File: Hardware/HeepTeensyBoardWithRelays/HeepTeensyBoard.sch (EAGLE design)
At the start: 40 parts, among them J1 MAGJACK, J4 POWER_JACKPTH, K1 RELAY-SPDT-JZC-11F, K2 RELAY-SPDT-JZC-11F, K3 RELAY-SPDT-JZC-11F, Q1 25MHz, U1 ENC28J60-SO

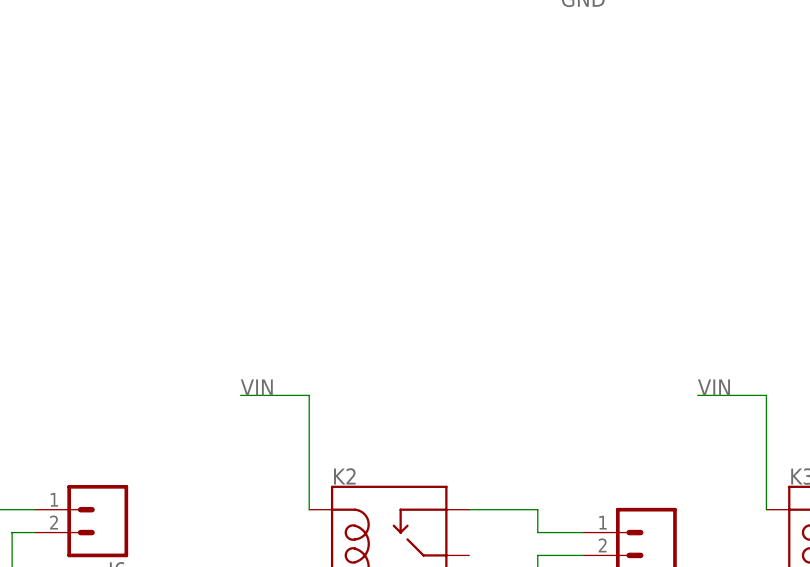
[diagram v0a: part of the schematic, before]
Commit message: #152 Added a label to the part of the schematic with AC inputs
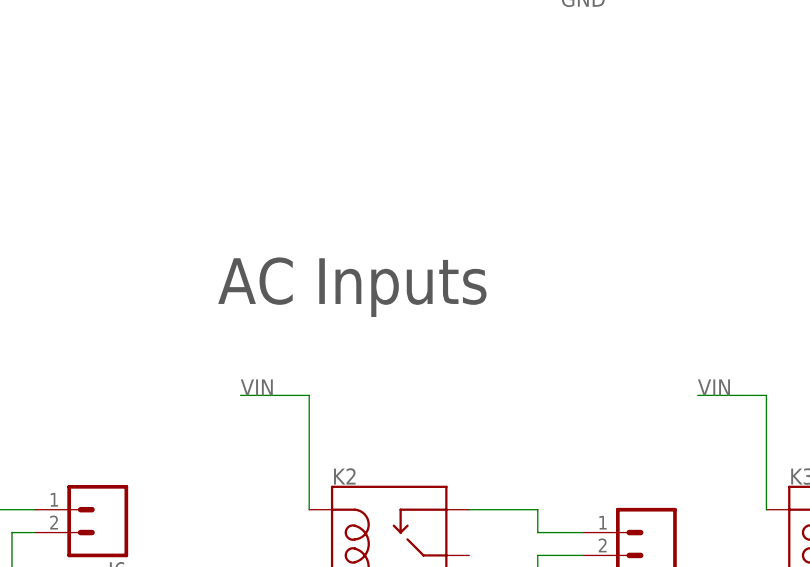
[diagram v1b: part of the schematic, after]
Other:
- note added: "AC Inputs"
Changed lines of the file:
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@@
 <text x="175.26" y="111.76" size="2.54" layer="97">Power LED</text>
 <text x="162.56" y="45.72" size="2.54" layer="97">Power Inputs</text>
+<text x="149.86" y="-33.02" size="5.08" layer="97">AC Inputs</text>
 </plain>
 <instances>

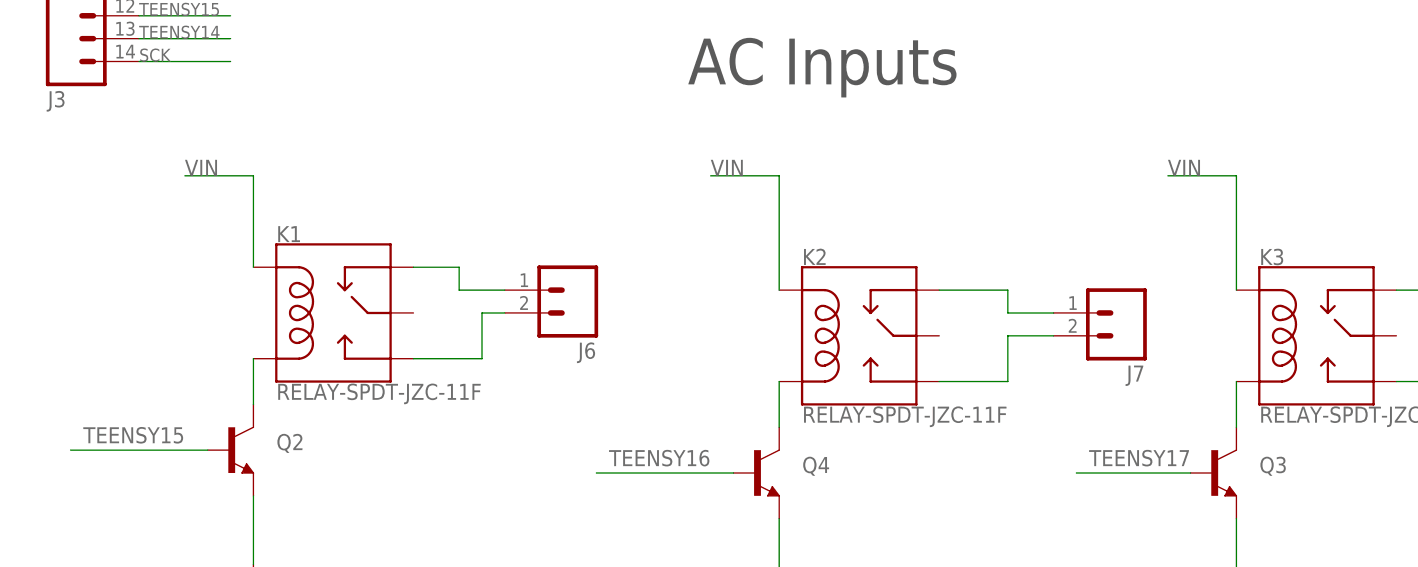
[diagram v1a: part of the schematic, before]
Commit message: #152 Added filtering capacitor to AC inputs
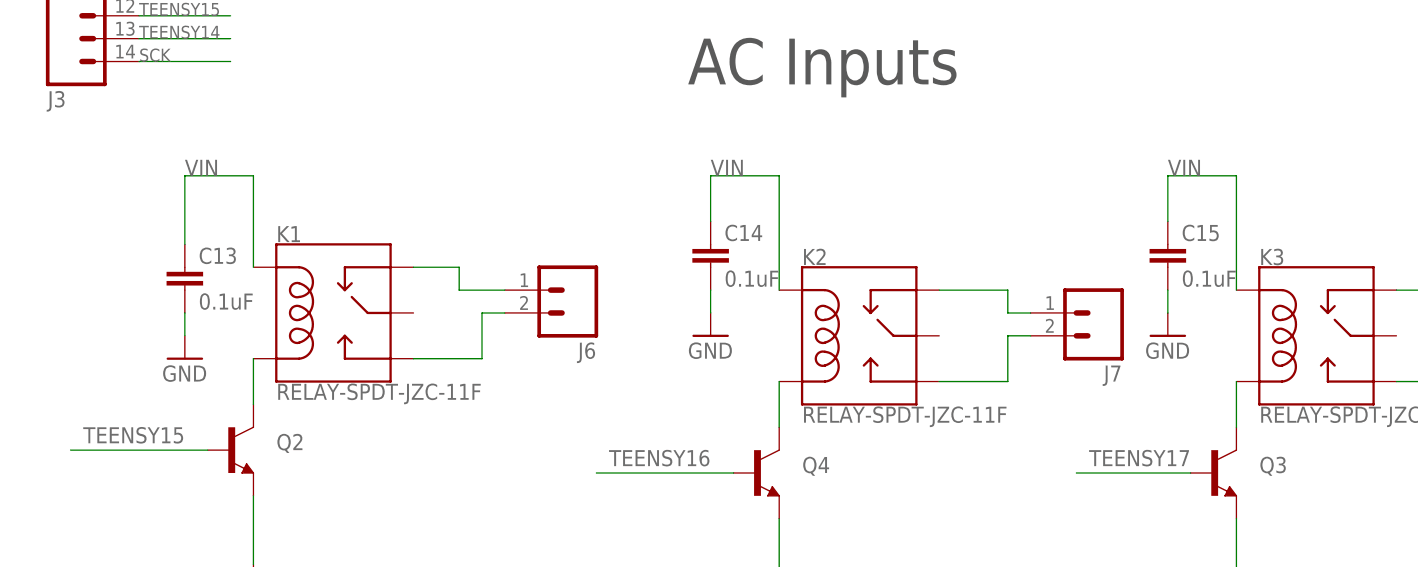
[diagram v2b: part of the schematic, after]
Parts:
- added C13, C14, C15: 0.1uF, SparkFun-Capacitors:CAP0603-CAP
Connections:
- net GND: now also C13.2, C14.2, C15.2
- net VIN: now also C13.1, C14.1, C15.1
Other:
- moved on the sheet: J7
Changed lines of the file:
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@@
 <part name="J7" library="SparkFun-Connectors" deviceset="M02" device="5MM"/>
 <part name="J8" library="SparkFun-Connectors" deviceset="M02" device="5MM"/>
+<part name="C13" library="SparkFun-Capacitors" deviceset="CAP" device="0603-CAP" value="0.1uF"/>
+<part name="GND18" library="SparkFun-Aesthetics" deviceset="GND" device=""/>
+<part name="C14" library="SparkFun-Capacitors" deviceset="CAP" device="0603-CAP" value="0.1uF"/>
+<part name="GND19" library="SparkFun-Aesthetics" deviceset="GND" device=""/>
+<part name="C15" library="SparkFun-Capacitors" deviceset="CAP" device="0603-CAP" value="0.1uF"/>
+<part name="GND20" library="SparkFun-Aesthetics" deviceset="GND" device=""/>
 </parts>
 <sheets>
@@
 <instance part="GND17" gate="1" x="210.82" y="-91.44"/>
 <instance part="J6" gate="G$1" x="137.16" y="-55.88" rot="R180"/>
-<instance part="J7" gate="G$1" x="198.12" y="-58.42" rot="R180"/>
+<instance part="J7" gate="G$1" x="195.58" y="-58.42" rot="R180"/>
 <instance part="J8" gate="G$1" x="248.92" y="-58.42" rot="R180"/>
+<instance part="C13" gate="G$1" x="93.98" y="-55.88"/>
+<instance part="GND18" gate="1" x="93.98" y="-63.5"/>
+<instance part="C14" gate="G$1" x="152.4" y="-53.34"/>
+<instance part="GND19" gate="1" x="152.4" y="-60.96"/>
+<instance part="C15" gate="G$1" x="203.2" y="-53.34"/>
+<instance part="GND20" gate="1" x="203.2" y="-60.96"/>
 </instances>
 <busses>
@@
 <wire x1="210.82" y1="-81.28" x2="210.82" y2="-88.9" width="0.1524" layer="91"/>
 <pinref part="GND17" gate="1" pin="GND"/>
+</segment>
+<segment>
+<pinref part="C13" gate="G$1" pin="2"/>
+<wire x1="93.98" y1="-58.42" x2="93.98" y2="-60.96" width="0.1524" layer="91"/>
+<pinref part="GND18" gate="1" pin="GND"/>
+</segment>
+<segment>
+<pinref part="C14" gate="G$1" pin="2"/>
+<wire x1="152.4" y1="-55.88" x2="152.4" y2="-58.42" width="0.1524" layer="91"/>
+<pinref part="GND19" gate="1" pin="GND"/>
+</segment>
+<segment>
+<pinref part="C15" gate="G$1" pin="2"/>
+<wire x1="203.2" y1="-55.88" x2="203.2" y2="-58.42" width="0.1524" layer="91"/>
+<pinref part="GND20" gate="1" pin="GND"/>
 </segment>
 </net>
@@
 <wire x1="101.6" y1="-43.18" x2="93.98" y2="-43.18" width="0.1524" layer="91"/>
 <label x="93.98" y="-43.18" size="1.778" layer="95"/>
+<wire x1="93.98" y1="-43.18" x2="93.98" y2="-50.8" width="0.1524" layer="91"/>
+<pinref part="C13" gate="G$1" pin="1"/>
 </segment>
 <segment>
@@
 <wire x1="160.02" y1="-43.18" x2="152.4" y2="-43.18" width="0.1524" layer="91"/>
 <label x="152.4" y="-43.18" size="1.778" layer="95"/>
+<wire x1="152.4" y1="-43.18" x2="152.4" y2="-48.26" width="0.1524" layer="91"/>
+<pinref part="C14" gate="G$1" pin="1"/>
 </segment>
 <segment>
@@
 <wire x1="210.82" y1="-43.18" x2="203.2" y2="-43.18" width="0.1524" layer="91"/>
 <label x="203.2" y="-43.18" size="1.778" layer="95"/>
+<wire x1="203.2" y1="-43.18" x2="203.2" y2="-48.26" width="0.1524" layer="91"/>
+<pinref part="C15" gate="G$1" pin="1"/>
 </segment>
 </net>
@@
 <wire x1="185.42" y1="-55.88" x2="185.42" y2="-58.42" width="0.1524" layer="91"/>
 <pinref part="J7" gate="G$1" pin="1"/>
-<wire x1="185.42" y1="-58.42" x2="190.5" y2="-58.42" width="0.1524" layer="91"/>
+<wire x1="185.42" y1="-58.42" x2="187.96" y2="-58.42" width="0.1524" layer="91"/>
 </segment>
 </net>
@@
 <segment>
 <pinref part="J7" gate="G$1" pin="2"/>
-<wire x1="190.5" y1="-60.96" x2="185.42" y2="-60.96" width="0.1524" layer="91"/>
+<wire x1="187.96" y1="-60.96" x2="185.42" y2="-60.96" width="0.1524" layer="91"/>
 <wire x1="185.42" y1="-60.96" x2="185.42" y2="-66.04" width="0.1524" layer="91"/>
 <pinref part="K2" gate="K$1" pin="NO"/>

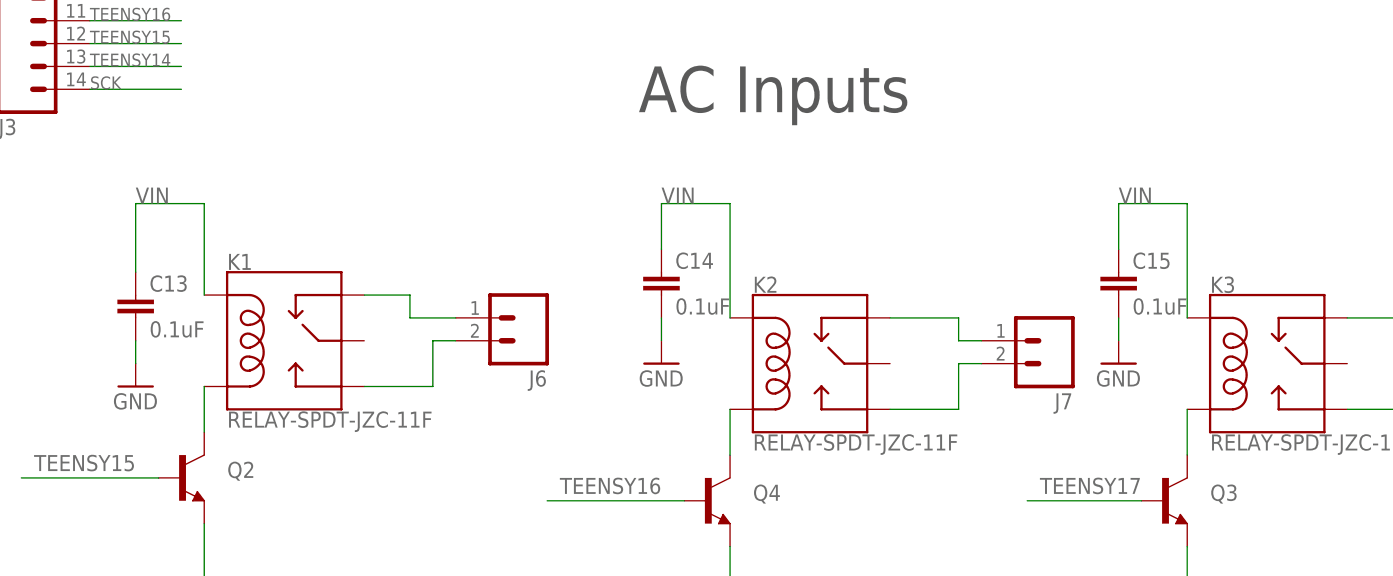
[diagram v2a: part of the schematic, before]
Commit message: #152 Added kick back diodes to the relay circuits
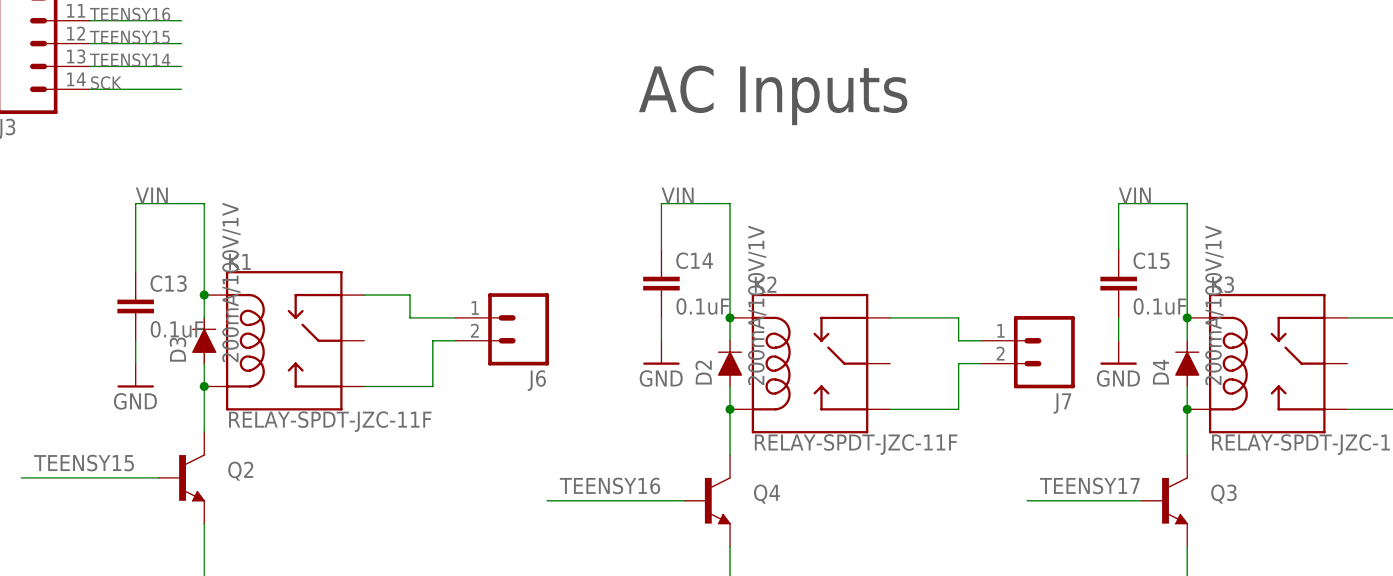
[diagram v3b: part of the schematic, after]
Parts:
- added D2, D3, D4: 200mA/100V/1V, SparkFun-DiscreteSemi:DIODE-1N4148
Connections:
- net N$11: now also D2.A
- net N$14: now also D4.A
- net N$9: now also D3.A
- net VIN: now also D2.C, D3.C, D4.C
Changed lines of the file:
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@@
 <part name="C15" library="SparkFun-Capacitors" deviceset="CAP" device="0603-CAP" value="0.1uF"/>
 <part name="GND20" library="SparkFun-Aesthetics" deviceset="GND" device=""/>
+<part name="D2" library="SparkFun-DiscreteSemi" deviceset="DIODE" device="-1N4148" value="200mA/100V/1V"/>
+<part name="D3" library="SparkFun-DiscreteSemi" deviceset="DIODE" device="-1N4148" value="200mA/100V/1V"/>
+<part name="D4" library="SparkFun-DiscreteSemi" deviceset="DIODE" device="-1N4148" value="200mA/100V/1V"/>
 </parts>
 <sheets>
@@
 <instance part="C15" gate="G$1" x="203.2" y="-53.34"/>
 <instance part="GND20" gate="1" x="203.2" y="-60.96"/>
+<instance part="D2" gate="G$1" x="160.02" y="-60.96" rot="R90"/>
+<instance part="D3" gate="G$1" x="101.6" y="-58.42" rot="R90"/>
+<instance part="D4" gate="G$1" x="210.82" y="-60.96" rot="R90"/>
 </instances>
 <busses>
@@
 <wire x1="93.98" y1="-43.18" x2="93.98" y2="-50.8" width="0.1524" layer="91"/>
 <pinref part="C13" gate="G$1" pin="1"/>
+<pinref part="D3" gate="G$1" pin="C"/>
+<wire x1="101.6" y1="-55.88" x2="101.6" y2="-53.34" width="0.1524" layer="91"/>
+<junction x="101.6" y="-53.34"/>
 </segment>
 <segment>
@@
 <wire x1="152.4" y1="-43.18" x2="152.4" y2="-48.26" width="0.1524" layer="91"/>
 <pinref part="C14" gate="G$1" pin="1"/>
+<pinref part="D2" gate="G$1" pin="C"/>
+<wire x1="160.02" y1="-58.42" x2="160.02" y2="-55.88" width="0.1524" layer="91"/>
+<junction x="160.02" y="-55.88"/>
 </segment>
 <segment>
@@
 <wire x1="203.2" y1="-43.18" x2="203.2" y2="-48.26" width="0.1524" layer="91"/>
 <pinref part="C15" gate="G$1" pin="1"/>
+<pinref part="D4" gate="G$1" pin="C"/>
+<wire x1="210.82" y1="-58.42" x2="210.82" y2="-55.88" width="0.1524" layer="91"/>
+<junction x="210.82" y="-55.88"/>
 </segment>
 </net>
@@
 <pinref part="K1" gate="K$1" pin="COIL2"/>
 <wire x1="101.6" y1="-68.58" x2="101.6" y2="-63.5" width="0.1524" layer="91"/>
+<pinref part="D3" gate="G$1" pin="A"/>
+<wire x1="101.6" y1="-63.5" x2="101.6" y2="-60.96" width="0.1524" layer="91"/>
+<junction x="101.6" y="-63.5"/>
 </segment>
 </net>
@@
 <pinref part="K2" gate="K$1" pin="COIL2"/>
 <wire x1="160.02" y1="-71.12" x2="160.02" y2="-66.04" width="0.1524" layer="91"/>
+<pinref part="D2" gate="G$1" pin="A"/>
+<wire x1="160.02" y1="-66.04" x2="160.02" y2="-63.5" width="0.1524" layer="91"/>
+<junction x="160.02" y="-66.04"/>
 </segment>
 </net>
@@
 <pinref part="K3" gate="K$1" pin="COIL2"/>
 <wire x1="210.82" y1="-71.12" x2="210.82" y2="-66.04" width="0.1524" layer="91"/>
-</segment>
-</net>
+<pinref part="D4" gate="G$1" pin="A"/>
+<wire x1="210.82" y1="-66.04" x2="210.82" y2="-63.5" width="0.1524" layer="91"/>
+<junction x="210.82" y="-66.04"/>
+</segment>
+</net>

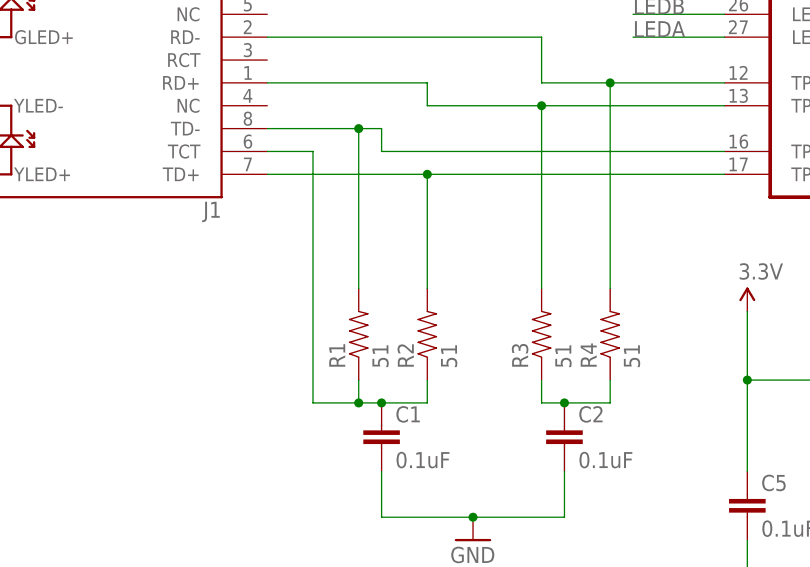
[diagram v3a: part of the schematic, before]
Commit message: #156 Added ferrite bead to schematic
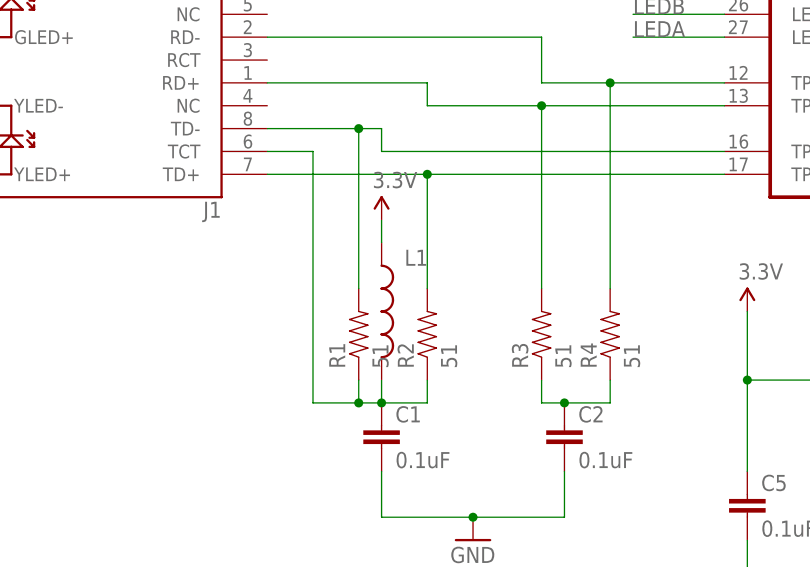
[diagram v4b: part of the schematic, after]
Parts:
- added L1: (no value), SparkFun-Passives:INDUCTOR0603
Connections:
- net 3.3V: now also L1.1
- net N$7: now also L1.2
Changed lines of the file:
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@@
 <part name="D3" library="SparkFun-DiscreteSemi" deviceset="DIODE" device="-1N4148" value="200mA/100V/1V"/>
 <part name="D4" library="SparkFun-DiscreteSemi" deviceset="DIODE" device="-1N4148" value="200mA/100V/1V"/>
+<part name="L1" library="SparkFun-Passives" deviceset="INDUCTOR" device="0603"/>
+<part name="SUPPLY6" library="SparkFun-Aesthetics" deviceset="3.3V" device=""/>
 </parts>
 <sheets>
@@
 <instance part="D3" gate="G$1" x="101.6" y="-58.42" rot="R90"/>
 <instance part="D4" gate="G$1" x="210.82" y="-60.96" rot="R90"/>
+<instance part="L1" gate="G$1" x="-96.52" y="35.56"/>
+<instance part="SUPPLY6" gate="G$1" x="-96.52" y="45.72"/>
 </instances>
 <busses>
@@
 <wire x1="-104.14" y1="25.4" x2="-99.06" y2="25.4" width="0.1524" layer="91"/>
 <junction x="-99.06" y="25.4"/>
+<pinref part="L1" gate="G$1" pin="2"/>
+<wire x1="-96.52" y1="27.94" x2="-96.52" y2="25.4" width="0.1524" layer="91"/>
 </segment>
 </net>
@@
 <pinref part="SUPPLY5" gate="G$1" pin="3.3V"/>
 </segment>
-</net>
+<segment>
+<pinref part="L1" gate="G$1" pin="1"/>
+<wire x1="-96.52" y1="43.18" x2="-96.52" y2="45.72" width="0.1524" layer="91"/>
+<pinref part="SUPPLY6" gate="G$1" pin="3.3V"/>
+</segment>
+</net>
